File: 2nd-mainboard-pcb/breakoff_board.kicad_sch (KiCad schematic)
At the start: 19 parts, among them J16 ISP, J18 Quartz, J23 Conn_01x04_Socket

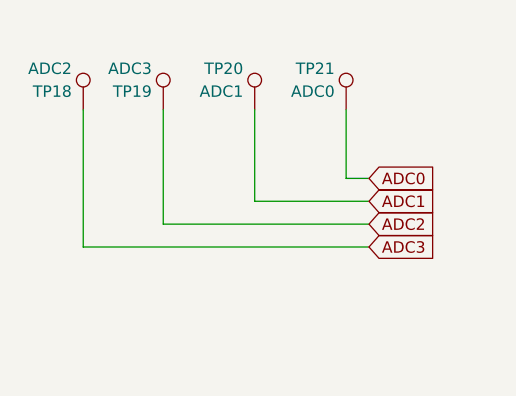
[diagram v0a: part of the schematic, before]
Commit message: Made traces thicker
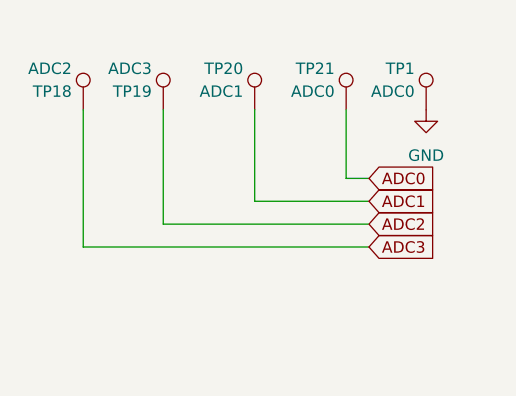
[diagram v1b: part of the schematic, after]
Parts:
- added TP1: ADC0, TestPoint:TestPoint_Pad_D2.0mm, symbol Connector:TestPoint
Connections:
- net GND: now also TP1.1
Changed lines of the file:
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@@
+	)
+	(symbol
+		(lib_id "Connector:TestPoint")
+		(at 201.93 31.75 0)
+		(mirror y)
+		(unit 1)
+		(exclude_from_sim no)
+		(in_bom yes)
+		(on_board yes)
+		(dnp no)
+		(property "Reference" "TP1"
+			(at 200.66 27.178 0)
+			(effects
+				(font
+					(size 1.27 1.27)
+				)
+				(justify left)
+			)
+		)
+		(property "Value" "ADC0"
+			(at 200.66 29.718 0)
+			(effects
+				(font
+					(size 1.27 1.27)
+				)
+				(justify left)
+			)
+		)
+		(property "Footprint" "TestPoint:TestPoint_Pad_D2.0mm"
+			(at 196.85 31.75 0)
+			(effects
+				(font
+					(size 1.27 1.27)
+				)
+				(hide yes)
+			)
+		)
+		(property "Datasheet" "~"
+			(at 196.85 31.75 0)
+			(effects
+				(font
+					(size 1.27 1.27)
+				)
+				(hide yes)
+			)
+		)
+		(property "Description" "test point"
+			(at 201.93 31.75 0)
+			(effects
+				(font
+					(size 1.27 1.27)
+				)
+				(hide yes)
+			)
+		)
+		(pin "1"
+		)
+		(instances
+			(project "2nd-mainboard-pcb"
+				(path "/6926a609-8b92-4b3a-88c8-3d023174b977/4a371be2-d5d9-4856-93da-432c037b0326"
+					(reference "TP1")
+					(unit 1)
+				)
+			)
+		)
 	)
 	(symbol
@@
 					(unit 1)
 				)
+			)
+		)
+	)
+	(symbol
+		(lib_id "power:GND")
+		(at 201.93 31.75 0)
+		(unit 1)
+		(exclude_from_sim no)
+		(in_bom yes)
+		(on_board yes)
+		(dnp no)
+		(fields_autoplaced yes)
+		(property "Reference" "#PWR070"
+			(at 201.93 38.1 0)
+			(effects
+				(font
+					(size 1.27 1.27)
+				)
+				(hide yes)
+			)
+		)
+		(property "Value" "GND"
+			(at 201.93 36.83 0)
+			(effects
+				(font
+					(size 1.27 1.27)
+				)
+			)
+		)
+		(property "Footprint" ""
+			(at 201.93 31.75 0)
+			(effects
+				(font
+					(size 1.27 1.27)
+				)
+				(hide yes)
+			)
+		)
+		(property "Datasheet" ""
+			(at 201.93 31.75 0)
+			(effects
+				(font
+					(size 1.27 1.27)
+				)
+				(hide yes)
+			)
+		)
+		(property "Description" "Power symbol creates a global label with name \"GND\" , ground"
+			(at 201.93 31.75 0)
+			(effects
+				(font
+					(size 1.27 1.27)
+				)
+				(hide yes)
+			)
+		)
+		(pin "1"
+		)
+		(instances
+			(project ""
+				(path "/6926a609-8b92-4b3a-88c8-3d023174b977/4a371be2-d5d9-4856-93da-432c037b0326"
+					(reference "#PWR070")
+					(unit 1)
+				)

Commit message: last few changes
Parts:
- removed J18: Quartz, Connector_PinSocket_2.54mm:PinSocket_1x02_P2.54mm_Vertical, symbol Connector:Conn_01x02_Socket
- removed TP22, TP23: I_Sense_5V, TestPoint:TestPoint_2Pads_Pitch2.54mm_Drill0.8mm, symbol Connector:TestPoint_2Pole
- removed TP25: I_Sense_12V, TestPoint:TestPoint_2Pads_Pitch2.54mm_Drill0.8mm, symbol Connector:TestPoint_2Pole
